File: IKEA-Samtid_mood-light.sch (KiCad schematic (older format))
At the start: 12 parts, among them IC1 ATMEGA168PA-A, P1 FTDI, P2 POWER

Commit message: Not enough free space for FTDI header :-(
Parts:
- added X1: CSTCE16M0V53-R0, symbol generic_resonator
- DS1: value 6A -> 757-CMS04TE12
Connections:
- wire segments 69 -> 72
- no-connect marks 19 -> 17
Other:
- note added: "Toshiba, 5A\napprox. SMA package"
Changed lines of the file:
@@
 Sheet 1 3
 Title "IKEA-Samtid_mood-light"
-Date "10 Jul 2014"
+Date "12 Jul 2014"
 Rev "0.10"
 Comp "2014 - blog.spitzenpfeil.org"
@@
 NoConn ~ 5200 1550
 NoConn ~ 5200 1450
-NoConn ~ 5300 2050
-NoConn ~ 5300 2150
 $Comp
 L PWR_FLAG #FLG011
@@
 P 5100 4850
 F 0 "DS1" H 5100 4950 40  0000 C CNN
-F 1 "6A" H 5100 4750 40  0000 C CNN
+F 1 "757-CMS04TE12" H 5100 4750 40  0000 C CNN
 F 2 "" H 5100 4850 60  0000 C CNN
 F 3 "" H 5100 4850 60  0000 C CNN
@@
 Wire Notes Line
 	3400 4400 3400 4550
+$Comp
+L generic_resonator X1
+U 1 1 53C088B5
+P 6200 1650
+F 0 "X1" H 6200 2000 60  0000 C CNN
+F 1 "CSTCE16M0V53-R0" H 6200 1900 60  0000 C CNN
+F 2 "" H 6200 1550 60  0000 C CNN
+F 3 "" H 6200 1550 60  0000 C CNN
+	1    6200 1650
+	1    0    0    -1
+$EndComp
+$Comp
+L GND #PWR017
+U 1 1 53C08AC4
+P 6200 2050
+F 0 "#PWR017" H 6200 2050 30  0001 C CNN
+F 1 "GND" H 6200 1980 30  0001 C CNN
+F 2 "" H 6200 2050 60  0000 C CNN
+F 3 "" H 6200 2050 60  0000 C CNN
+	1    6200 2050
+	1    0    0    -1
+$EndComp
+Wire Wire Line
+	6200 2000 6200 2050
+Text Label 5850 1650 3    60   ~ 0
+XTAL1
+Text Label 6550 1650 3    60   ~ 0
+XTAL2
+Wire Wire Line
+	6550 1550 6550 1650
+Wire Wire Line
+	5850 1550 5850 1650
+Text Notes 4850 5150 0    39   ~ 0
+Toshiba, 5A\napprox. SMA package
 $EndSCHEMATC

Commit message: Schematic: forgot change of 'TQFP-32' --> 'QFN32' for micro.
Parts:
- removed IC1: ATMEGA168PA-A, TQFP32, symbol ATMEGA168PA-A
- added IC1: ATMEGA168PA-M, MLF/QFN32, symbol ATMEGA168PA-M
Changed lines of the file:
@@
 Title "IKEA-Samtid_mood-light"
 Date "12 Jul 2014"
-Rev "0.10"
+Rev "0.11"
 Comp "2014 - blog.spitzenpfeil.org"
 Comment1 ""
@@
 Comment4 ""
 $EndDescr
-$Comp
-L ATMEGA168PA-A IC1
-U 1 1 53BED0DB
-P 4200 2550
-F 0 "IC1" H 3450 3800 40  0000 L BNN
-F 1 "ATMEGA168PA-A" H 4600 1150 40  0000 L BNN
-F 2 "TQFP32" H 4200 2550 30  0000 C CIN
-F 3 "" H 4200 2550 60  0000 C CNN
-	1    4200 2550
-	1    0    0    -1
-$EndComp
 $Comp
 L C C1
@@
 Text Notes 4850 5150 0    39   ~ 0
 Toshiba, 5A\napprox. SMA package
+$Comp
+L ATMEGA168PA-M IC1
+U 1 1 53C14D61
+P 4200 2550
+F 0 "IC1" H 3450 3800 40  0000 L BNN
+F 1 "ATMEGA168PA-M" H 4600 1150 40  0000 L BNN
+F 2 "MLF/QFN32" H 4200 2550 30  0000 C CIN
+F 3 "" H 4200 2550 60  0000 C CNN
+	1    4200 2550
+	1    0    0    -1
+$EndComp
 $EndSCHEMATC

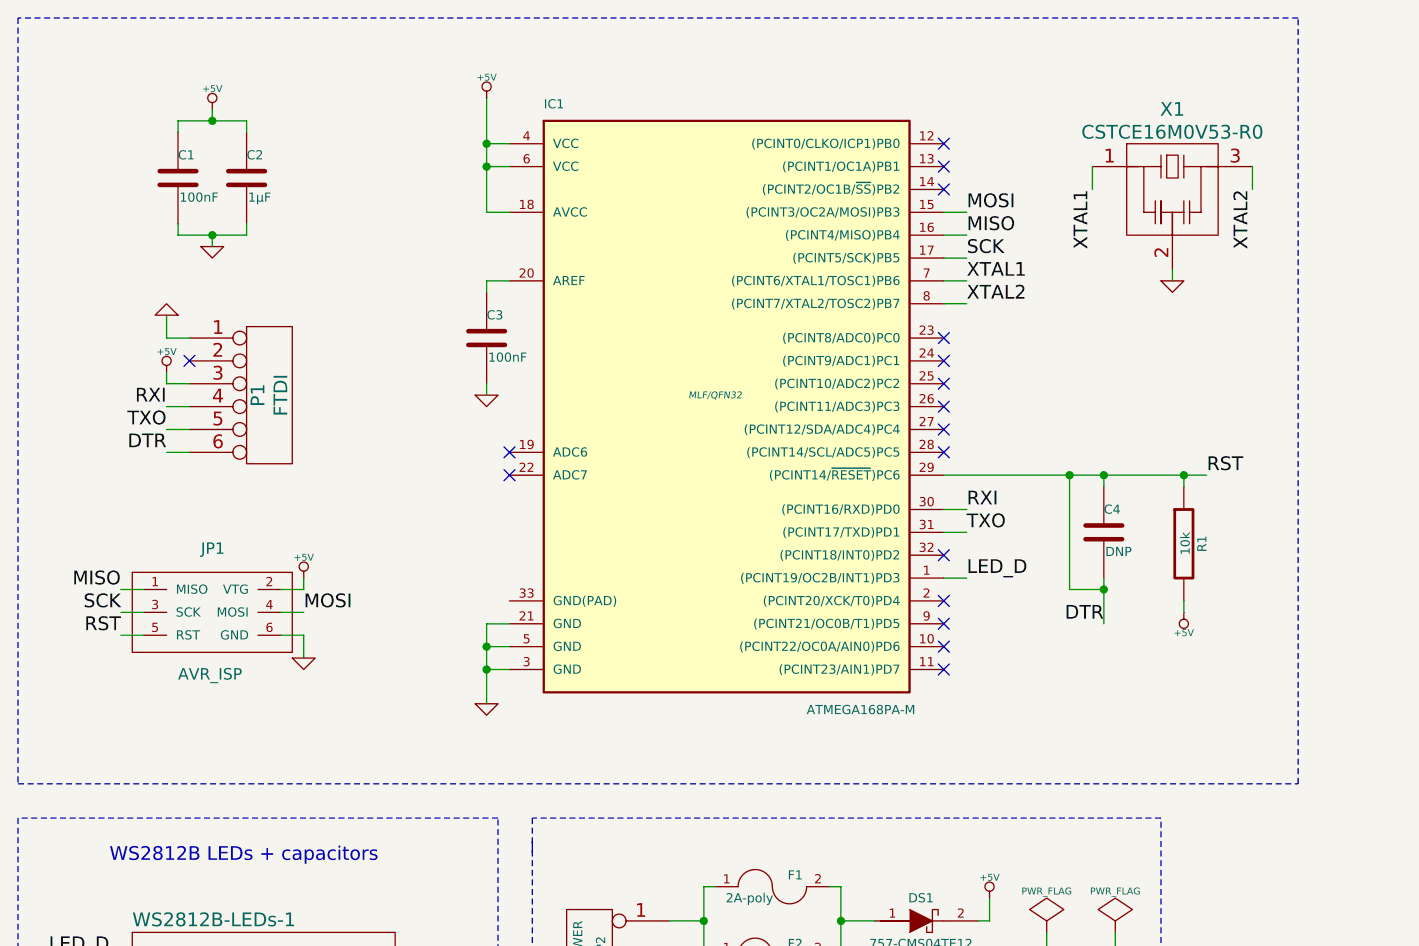
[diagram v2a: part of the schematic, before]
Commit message: Messing with µC board. Not so easy without board space.
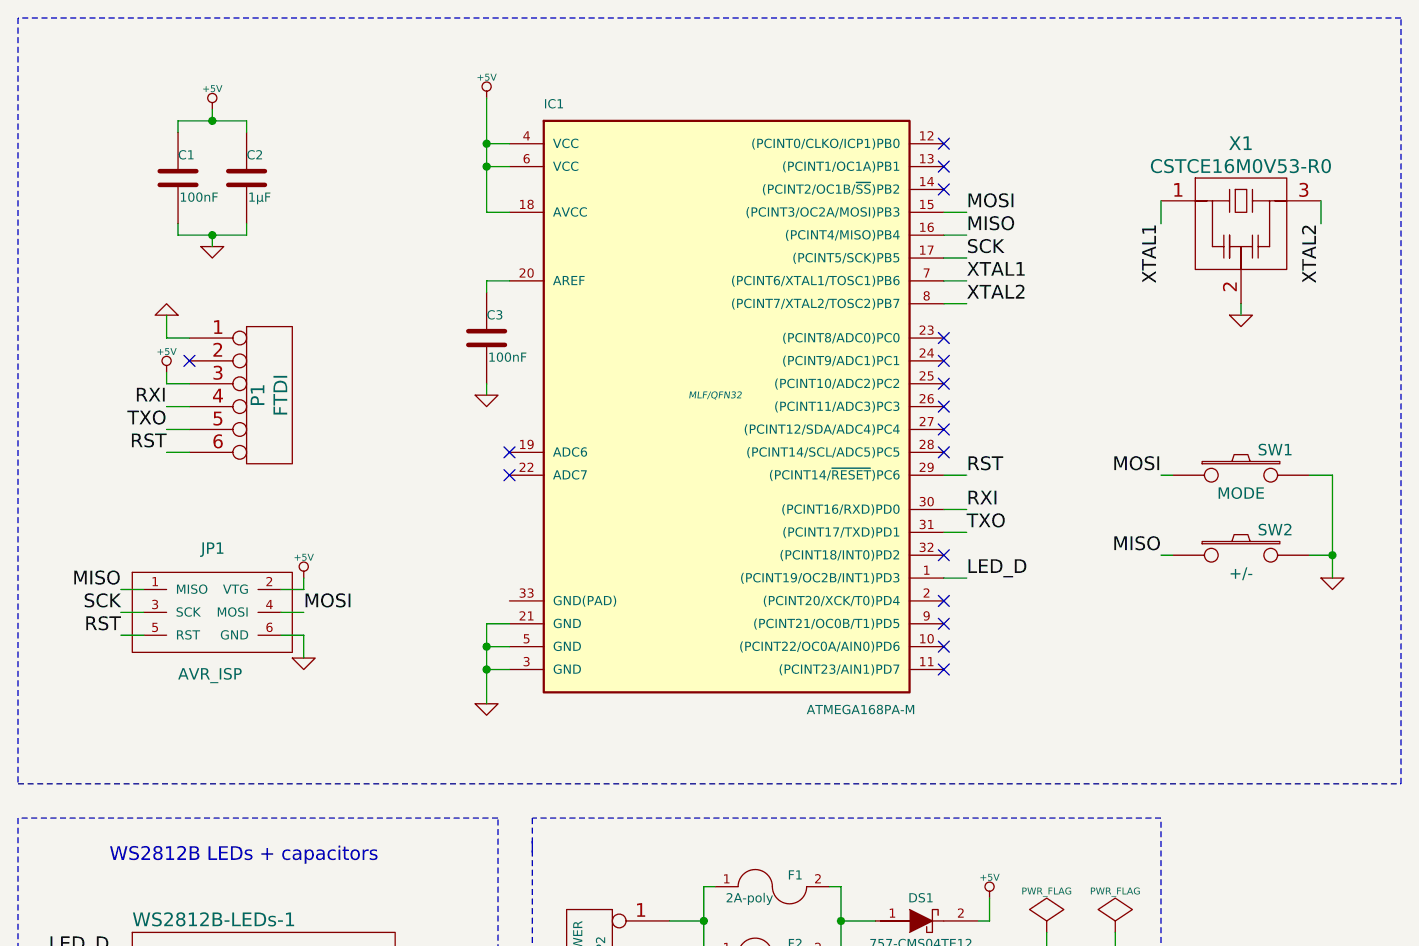
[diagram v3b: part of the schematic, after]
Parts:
- removed C4: DNP, symbol C
- removed R1: 10k, symbol R
- added SW1: MODE, symbol SW_PUSH
- added SW2: +/-, symbol SW_PUSH
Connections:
- net GND: now also SW1.2, SW2.2
- net MISO: now also SW2.1
- net MOSI: now also SW1.1
- net DTR renamed RST
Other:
- moved on the sheet: X1
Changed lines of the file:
@@
 Title "IKEA-Samtid_mood-light"
 Date "12 Jul 2014"
-Rev "0.11"
+Rev "0.13"
 Comp "2014 - blog.spitzenpfeil.org"
 Comment1 ""
@@
 TXO
 Text Label 1800 2800 2    60   ~ 0
-DTR
+RST
 Wire Wire Line
 	1800 2800 1900 2800
@@
 Wire Wire Line
 	1800 2600 1900 2600
-$Comp
-L C C4
-U 1 1 53BEDD52
-P 5900 3150
-F 0 "C4" H 5900 3250 40  0000 L CNN
-F 1 "DNP" H 5906 3065 40  0000 L CNN
-F 2 "" H 5938 3000 30  0000 C CNN
-F 3 "" H 5900 3150 60  0000 C CNN
-	1    5900 3150
-	1    0    0    -1
-$EndComp
-$Comp
-L R R1
-U 1 1 53BEDD93
-P 6250 3200
-F 0 "R1" V 6330 3200 40  0000 C CNN
-F 1 "10k" V 6257 3201 40  0000 C CNN
-F 2 "" V 6180 3200 30  0000 C CNN
-F 3 "" H 6250 3200 30  0000 C CNN
-	1    6250 3200
-	1    0    0    -1
-$EndComp
-$Comp
-L +5V #PWR07
-U 1 1 53BEDF97
-P 6250 3500
-F 0 "#PWR07" H 6250 3590 20  0001 C CNN
-F 1 "+5V" H 6250 3590 30  0000 C CNN
-F 2 "" H 6250 3500 60  0000 C CNN
-F 3 "" H 6250 3500 60  0000 C CNN
-	1    6250 3500
-	-1   0    0    1
-$EndComp
-Wire Wire Line
-	6250 3450 6250 3500
-Wire Wire Line
-	5900 2950 5900 2900
-Wire Wire Line
-	5200 2900 6350 2900
-Wire Wire Line
-	6250 2900 6250 2950
-Text Label 5900 3550 2    60   ~ 0
-DTR
-Wire Wire Line
-	5900 3350 5900 3550
-Connection ~ 5900 2900
-Connection ~ 5750 2900
-Wire Wire Line
-	5900 3400 5750 3400
-Wire Wire Line
-	5750 3400 5750 2900
-Connection ~ 5900 3400
 Text Label 5300 1850 0    60   ~ 0
 MISO
@@
 Wire Wire Line
 	5300 1750 5200 1750
-Text Label 6350 2900 0    60   ~ 0
+Text Label 5300 2900 0    60   ~ 0
 RST
-Connection ~ 6250 2900
-$Comp
-L GND #PWR08
+$Comp
+L GND #PWR07
 U 1 1 53BEE576
 P 3200 3900
-F 0 "#PWR08" H 3200 3900 30  0001 C CNN
+F 0 "#PWR07" H 3200 3900 30  0001 C CNN
 F 1 "GND" H 3200 3830 30  0001 C CNN
 F 2 "" H 3200 3900 60  0000 C CNN
@@
 Connection ~ 3200 3750
 $Comp
-L +5V #PWR09
+L +5V #PWR08
 U 1 1 53BEE6BA
 P 3200 1250
-F 0 "#PWR09" H 3200 1340 20  0001 C CNN
+F 0 "#PWR08" H 3200 1340 20  0001 C CNN
 F 1 "+5V" H 3200 1340 30  0000 C CNN
 F 2 "" H 3200 1250 60  0000 C CNN
@@
 $EndComp
 $Comp
-L GND #PWR010
+L GND #PWR09
 U 1 1 53BEE91C
 P 3200 2550
-F 0 "#PWR010" H 3200 2550 30  0001 C CNN
+F 0 "#PWR09" H 3200 2550 30  0001 C CNN
 F 1 "GND" H 3200 2480 30  0001 C CNN
 F 2 "" H 3200 2550 60  0000 C CNN
@@
 NoConn ~ 5200 1450
 $Comp
-L PWR_FLAG #FLG011
+L PWR_FLAG #FLG010
 U 1 1 53BF079C
 P 5650 4900
-F 0 "#FLG011" H 5650 4995 30  0001 C CNN
+F 0 "#FLG010" H 5650 4995 30  0001 C CNN
 F 1 "PWR_FLAG" H 5650 5080 30  0000 C CNN
 F 2 "" H 5650 4900 60  0000 C CNN
@@
 $EndComp
 $Comp
-L +5V #PWR012
+L +5V #PWR011
 U 1 1 53BF07F2
 P 5650 5000
-F 0 "#PWR012" H 5650 5090 20  0001 C CNN
+F 0 "#PWR011" H 5650 5090 20  0001 C CNN
 F 1 "+5V" H 5650 5090 30  0000 C CNN
 F 2 "" H 5650 5000 60  0000 C CNN
@@
 	5650 4900 5650 5000
 $Comp
-L GND #PWR013
+L GND #PWR012
 U 1 1 53BF092D
 P 5950 5050
-F 0 "#PWR013" H 5950 5050 30  0001 C CNN
+F 0 "#PWR012" H 5950 5050 30  0001 C CNN
 F 1 "GND" H 5950 4980 30  0001 C CNN
 F 2 "" H 5950 5050 60  0000 C CNN
@@
 $EndComp
 $Comp
-L PWR_FLAG #FLG014
+L PWR_FLAG #FLG013
 U 1 1 53BF0941
 P 5950 4900
-F 0 "#FLG014" H 5950 4995 30  0001 C CNN
+F 0 "#FLG013" H 5950 4995 30  0001 C CNN
 F 1 "PWR_FLAG" H 5950 5080 30  0000 C CNN
 F 2 "" H 5950 4900 60  0000 C CNN
@@
 	1150 900  1150 4250
 Wire Notes Line
-	1150 4250 6750 4250
-Wire Notes Line
-	6750 4250 6750 900
-Wire Notes Line
-	6750 900  1150 900
+	1150 4250 7200 4250
+Wire Notes Line
+	7200 4250 7200 900
+Wire Notes Line
+	7200 900  1150 900
 $Comp
 L CONN_2 P2
@@
 $EndComp
 $Comp
-L +5V #PWR015
+L +5V #PWR014
 U 1 1 53C34107
 P 5400 4750
-F 0 "#PWR015" H 5400 4840 20  0001 C CNN
+F 0 "#PWR014" H 5400 4840 20  0001 C CNN
 F 1 "+5V" H 5400 4840 30  0000 C CNN
 F 2 "" H 5400 4750 60  0000 C CNN
@@
 	4150 4700 4150 5000
 $Comp
-L GND #PWR016
+L GND #PWR015
 U 1 1 53C340CF
 P 4050 5200
-F 0 "#PWR016" H 4050 5200 30  0001 C CNN
+F 0 "#PWR015" H 4050 5200 30  0001 C CNN
 F 1 "GND" H 4050 5130 30  0001 C CNN
 F 2 "" H 4050 5200 60  0000 C CNN
@@
 L generic_resonator X1
 U 1 1 53C088B5
-P 6200 1650
-F 0 "X1" H 6200 2000 60  0000 C CNN
-F 1 "CSTCE16M0V53-R0" H 6200 1900 60  0000 C CNN
-F 2 "" H 6200 1550 60  0000 C CNN
-F 3 "" H 6200 1550 60  0000 C CNN
-	1    6200 1650
-	1    0    0    -1
-$EndComp
-$Comp
-L GND #PWR017
+P 6500 1800
+F 0 "X1" H 6500 2150 60  0000 C CNN
+F 1 "CSTCE16M0V53-R0" H 6500 2050 60  0000 C CNN
+F 2 "" H 6500 1700 60  0000 C CNN
+F 3 "" H 6500 1700 60  0000 C CNN
+	1    6500 1800
+	1    0    0    -1
+$EndComp
+$Comp
+L GND #PWR016
 U 1 1 53C08AC4
-P 6200 2050
-F 0 "#PWR017" H 6200 2050 30  0001 C CNN
-F 1 "GND" H 6200 1980 30  0001 C CNN
-F 2 "" H 6200 2050 60  0000 C CNN
-F 3 "" H 6200 2050 60  0000 C CNN
-	1    6200 2050
-	1    0    0    -1
-$EndComp
-Wire Wire Line
-	6200 2000 6200 2050
-Text Label 5850 1650 3    60   ~ 0
+P 6500 2200
+F 0 "#PWR016" H 6500 2200 30  0001 C CNN
+F 1 "GND" H 6500 2130 30  0001 C CNN
+F 2 "" H 6500 2200 60  0000 C CNN
+F 3 "" H 6500 2200 60  0000 C CNN
+	1    6500 2200
+	1    0    0    -1
+$EndComp
+Wire Wire Line
+	6500 2150 6500 2200
+Text Label 6150 1800 3    60   ~ 0
 XTAL1
-Text Label 6550 1650 3    60   ~ 0
+Text Label 6850 1800 3    60   ~ 0
 XTAL2
 Wire Wire Line
-	6550 1550 6550 1650
-Wire Wire Line
-	5850 1550 5850 1650
+	6850 1700 6850 1800
+Wire Wire Line
+	6150 1700 6150 1800
 Text Notes 4850 5150 0    39   ~ 0
 Toshiba, 5A\napprox. SMA package
@@
 	1    0    0    -1
 $EndComp
+Wire Wire Line
+	5200 2900 5300 2900
+$Comp
+L SW_PUSH SW1
+U 1 1 53C15F1B
+P 6500 2900
+F 0 "SW1" H 6650 3010 50  0000 C CNN
+F 1 "MODE" H 6500 2820 50  0000 C CNN
+F 2 "" H 6500 2900 60  0000 C CNN
+F 3 "" H 6500 2900 60  0000 C CNN
+	1    6500 2900
+	1    0    0    -1
+$EndComp
+$Comp
+L SW_PUSH SW2
+U 1 1 53C15FEF
+P 6500 3250
+F 0 "SW2" H 6650 3360 50  0000 C CNN
+F 1 "+/-" H 6500 3170 50  0000 C CNN
+F 2 "" H 6500 3250 60  0000 C CNN
+F 3 "" H 6500 3250 60  0000 C CNN
+	1    6500 3250
+	1    0    0    -1
+$EndComp
+Wire Wire Line
+	6800 2900 6900 2900
+Wire Wire Line
+	6900 2900 6900 3350
+Wire Wire Line
+	6900 3250 6800 3250
+Connection ~ 6900 3250
+$Comp
+L GND #PWR017
+U 1 1 53C16191
+P 6900 3350
+F 0 "#PWR017" H 6900 3350 30  0001 C CNN
+F 1 "GND" H 6900 3280 30  0001 C CNN
+F 2 "" H 6900 3350 60  0000 C CNN
+F 3 "" H 6900 3350 60  0000 C CNN
+	1    6900 3350
+	1    0    0    -1
+$EndComp
+Text Label 6150 2900 2    60   ~ 0
+MOSI
+Text Label 6150 3250 2    60   ~ 0
+MISO
+Wire Wire Line
+	6150 2900 6200 2900
+Wire Wire Line
+	6150 3250 6200 3250
 $EndSCHEMATC

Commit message: Getting there...
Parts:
- added P3: MCU-Board, symbol CONN_6
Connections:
- net +5V: now also P3.3
- net GND: now also P3.1
- net LED_D: no longer names the net of IC1.1 ((PCINT19/OC2B/INT1)PD3)
- new net TXO/LEDs: P3.5
- no-connect marks 17 -> 21
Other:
- note added: "MCU-Board (female)"
- note added: "MCU-Board (male)"
- moved on the sheet: DS1, F1, F2, JP1, P2

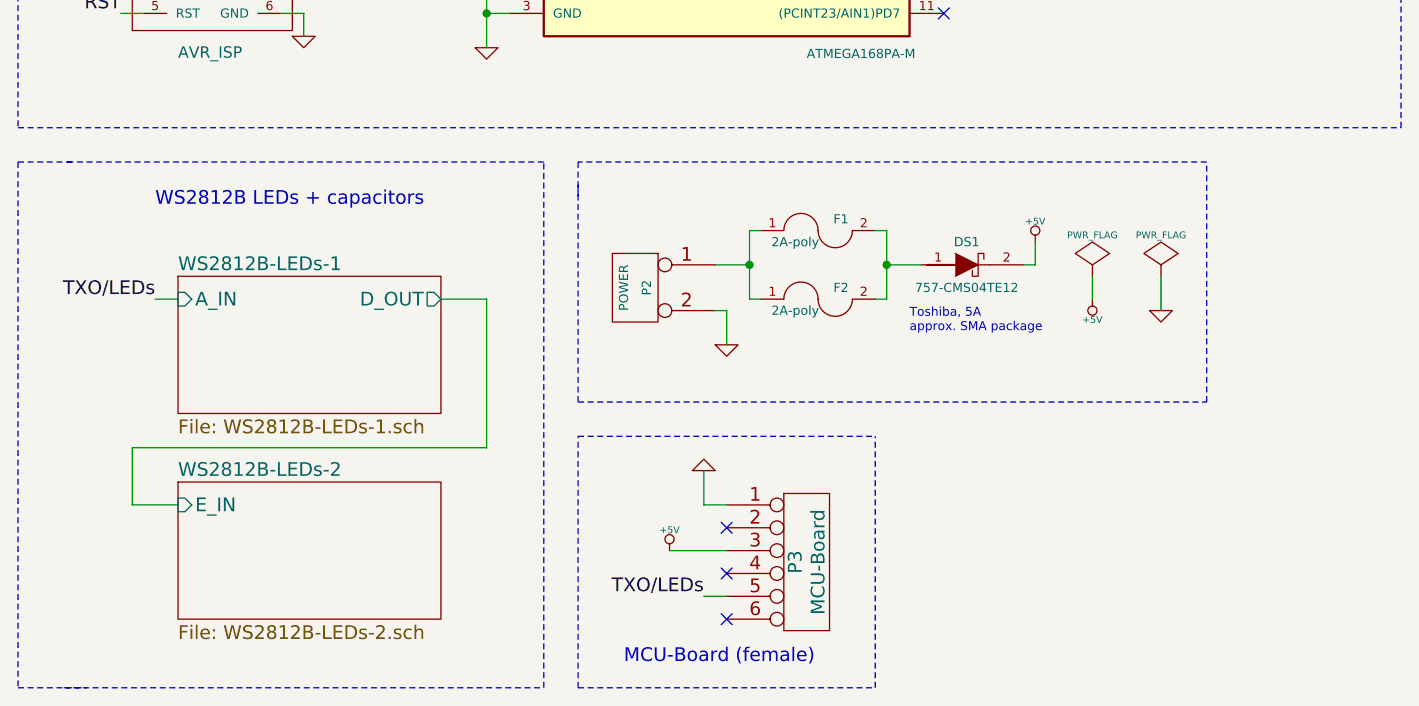
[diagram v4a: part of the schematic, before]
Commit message: Put 150R in LED data line.
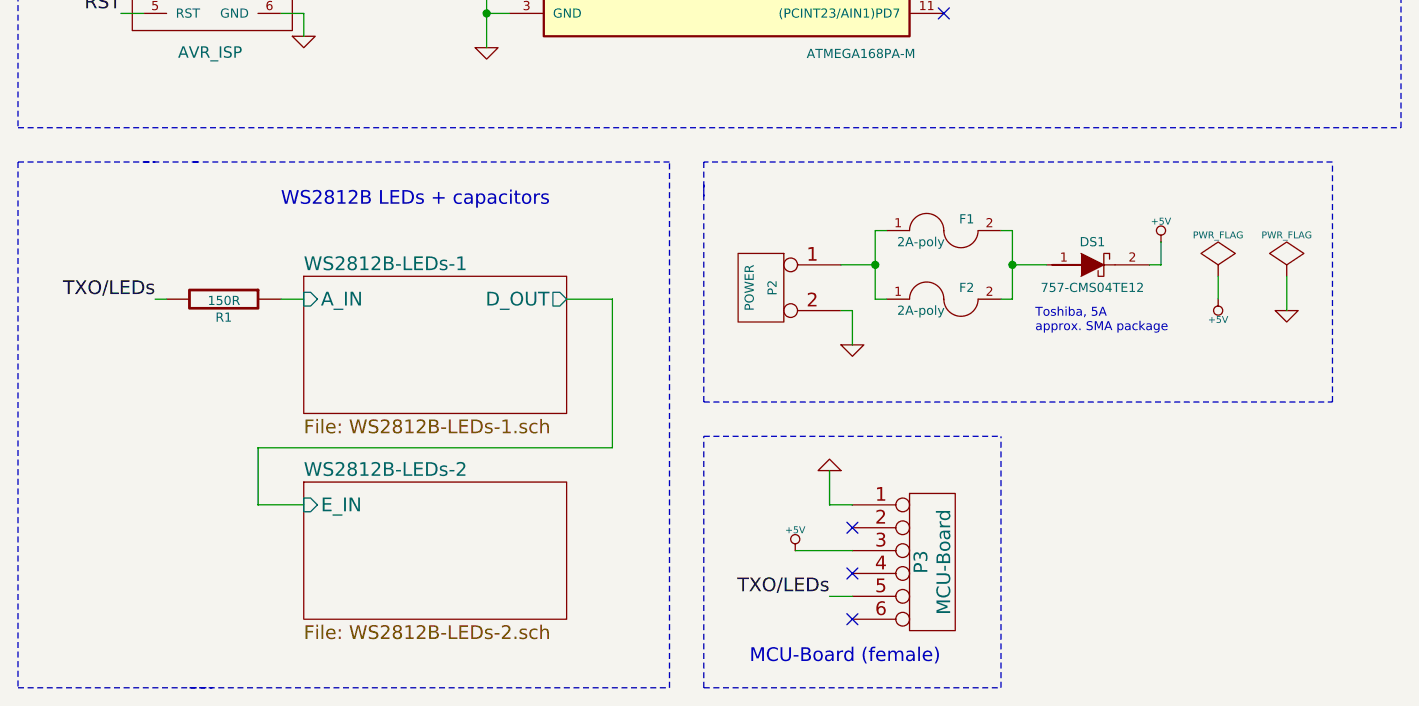
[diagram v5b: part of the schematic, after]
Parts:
- added R1: 150R, symbol R
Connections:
- net TXO/LEDs: now also R1.2
- new net WS2812B-LEDs-1/A_IN: R1.1
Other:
- moved on the sheet: DS1, F1, F2, P2, P3
